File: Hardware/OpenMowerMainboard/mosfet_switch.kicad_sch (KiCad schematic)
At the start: 5 parts, among them Q5 BSS138, Q6 Q_PMOS_GDS

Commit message: wip schematic
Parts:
- renumbered Q5 to Q7, Q6 to Q8, R26 to R29, R27 to R30, R28 to R31
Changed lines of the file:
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@@
   (symbol (lib_id "Device:R") (at 107.95 97.79 0)
     (in_bom yes) (on_board yes) (fields_autoplaced)
-    (property "Reference" "R26" (id 0) (at 110.49 96.5199 0)
+    (property "Reference" "R29" (id 0) (at 110.49 96.5199 0)
       (effects (font (size 1.27 1.27)) (justify left))
     )
@@
   (symbol (lib_id "Device:R") (at 114.3 90.17 90)
     (in_bom yes) (on_board yes) (fields_autoplaced)
-    (property "Reference" "R27" (id 0) (at 114.3 83.82 90))
+    (property "Reference" "R30" (id 0) (at 114.3 83.82 90))
     (property "Value" "R" (id 1) (at 114.3 86.36 90))
     (property "Footprint" "Resistor_SMD:R_0805_2012Metric" (id 2) (at 114.3 91.948 90)
@@
   (symbol (lib_id "Device:Q_PMOS_GDS") (at 135.89 80.01 0)
     (in_bom yes) (on_board yes) (fields_autoplaced)
-    (property "Reference" "Q6" (id 0) (at 142.24 78.7399 0)
+    (property "Reference" "Q8" (id 0) (at 142.24 78.7399 0)
       (effects (font (size 1.27 1.27)) (justify left))
     )
@@
   (symbol (lib_id "Transistor_FET:BSS138") (at 125.73 90.17 0)
     (in_bom yes) (on_board yes) (fields_autoplaced)
-    (property "Reference" "Q5" (id 0) (at 132.08 88.8999 0)
+    (property "Reference" "Q7" (id 0) (at 132.08 88.8999 0)
       (effects (font (size 1.27 1.27)) (justify left))
     )
@@
   (symbol (lib_id "Device:R") (at 128.27 71.12 0)
     (in_bom yes) (on_board yes) (fields_autoplaced)
-    (property "Reference" "R28" (id 0) (at 130.81 69.8499 0)
+    (property "Reference" "R31" (id 0) (at 130.81 69.8499 0)
       (effects (font (size 1.27 1.27)) (justify left))
     )

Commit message: added footprints to schematic
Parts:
- R29, R30, R31: footprint Resistor_SMD:R_0805_2012Metric -> Resistor_SMD:R_0805_2012Metric_Pad1.20x1.40mm_HandSolder
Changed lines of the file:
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@@
       (effects (font (size 1.27 1.27)) (justify left))
     )
-    (property "Footprint" "Resistor_SMD:R_0805_2012Metric" (id 2) (at 106.172 97.79 90)
+    (property "Footprint" "Resistor_SMD:R_0805_2012Metric_Pad1.20x1.40mm_HandSolder" (id 2) (at 106.172 97.79 90)
       (effects (font (size 1.27 1.27)) hide)
     )
@@
     (property "Reference" "R30" (id 0) (at 114.3 83.82 90))
     (property "Value" "R" (id 1) (at 114.3 86.36 90))
-    (property "Footprint" "Resistor_SMD:R_0805_2012Metric" (id 2) (at 114.3 91.948 90)
+    (property "Footprint" "Resistor_SMD:R_0805_2012Metric_Pad1.20x1.40mm_HandSolder" (id 2) (at 114.3 91.948 90)
       (effects (font (size 1.27 1.27)) hide)
     )
@@
       (effects (font (size 1.27 1.27)) (justify left))
     )
-    (property "Footprint" "Resistor_SMD:R_0805_2012Metric" (id 2) (at 126.492 71.12 90)
+    (property "Footprint" "Resistor_SMD:R_0805_2012Metric_Pad1.20x1.40mm_HandSolder" (id 2) (at 126.492 71.12 90)
       (effects (font (size 1.27 1.27)) hide)
     )

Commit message: wip
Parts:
- renumbered Q7 to Q5, Q8 to Q6, R29 to R26, R30 to R27, R31 to R28
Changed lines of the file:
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@@
   (symbol (lib_id "Device:R") (at 107.95 97.79 0)
     (in_bom yes) (on_board yes) (fields_autoplaced)
-    (property "Reference" "R29" (id 0) (at 110.49 96.5199 0)
+    (property "Reference" "R26" (id 0) (at 110.49 96.5199 0)
       (effects (font (size 1.27 1.27)) (justify left))
     )
@@
   (symbol (lib_id "Device:R") (at 114.3 90.17 90)
     (in_bom yes) (on_board yes) (fields_autoplaced)
-    (property "Reference" "R30" (id 0) (at 114.3 83.82 90))
+    (property "Reference" "R27" (id 0) (at 114.3 83.82 90))
     (property "Value" "R" (id 1) (at 114.3 86.36 90))
     (property "Footprint" "Resistor_SMD:R_0805_2012Metric_Pad1.20x1.40mm_HandSolder" (id 2) (at 114.3 91.948 90)
@@
   (symbol (lib_id "Device:Q_PMOS_GDS") (at 135.89 80.01 0)
     (in_bom yes) (on_board yes) (fields_autoplaced)
-    (property "Reference" "Q8" (id 0) (at 142.24 78.7399 0)
+    (property "Reference" "Q6" (id 0) (at 142.24 78.7399 0)
       (effects (font (size 1.27 1.27)) (justify left))
     )
@@
   (symbol (lib_id "Transistor_FET:BSS138") (at 125.73 90.17 0)
     (in_bom yes) (on_board yes) (fields_autoplaced)
-    (property "Reference" "Q7" (id 0) (at 132.08 88.8999 0)
+    (property "Reference" "Q5" (id 0) (at 132.08 88.8999 0)
       (effects (font (size 1.27 1.27)) (justify left))
     )
@@
   (symbol (lib_id "Device:R") (at 128.27 71.12 0)
     (in_bom yes) (on_board yes) (fields_autoplaced)
-    (property "Reference" "R31" (id 0) (at 130.81 69.8499 0)
+    (property "Reference" "R28" (id 0) (at 130.81 69.8499 0)
       (effects (font (size 1.27 1.27)) (justify left))
     )

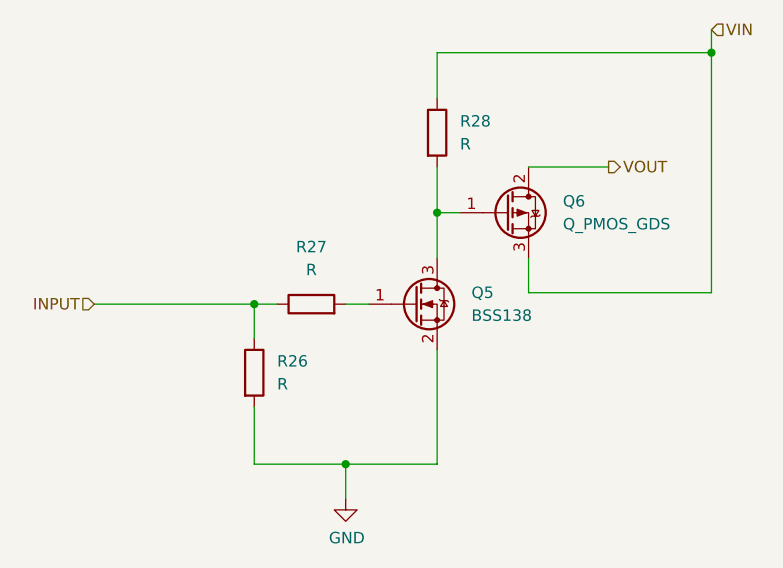
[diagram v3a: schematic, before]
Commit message: update Resistance Values
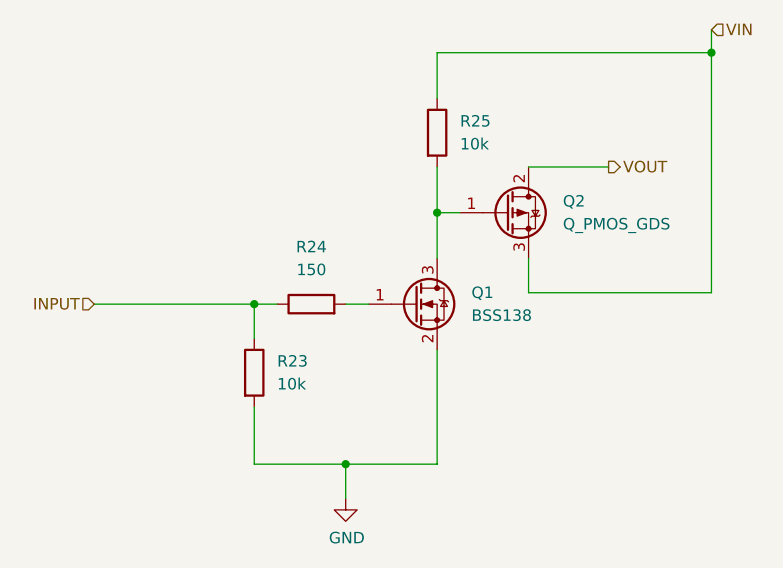
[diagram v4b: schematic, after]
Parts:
- R23: renamed from R26; value R -> 10k
- R24: renamed from R27; value R -> 150
- R25: renamed from R28; value R -> 10k
- renumbered Q5 to Q1, Q6 to Q2
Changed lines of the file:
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@@
   (symbol (lib_id "Device:R") (at 107.95 97.79 0)
     (in_bom yes) (on_board yes) (fields_autoplaced)
-    (property "Reference" "R26" (id 0) (at 110.49 96.5199 0)
+    (property "Reference" "R23" (id 0) (at 110.49 96.5199 0)
       (effects (font (size 1.27 1.27)) (justify left))
     )
-    (property "Value" "R" (id 1) (at 110.49 99.0599 0)
+    (property "Value" "10k" (id 1) (at 110.49 99.0599 0)
       (effects (font (size 1.27 1.27)) (justify left))
     )
@@
   (symbol (lib_id "Device:R") (at 114.3 90.17 90)
     (in_bom yes) (on_board yes) (fields_autoplaced)
-    (property "Reference" "R27" (id 0) (at 114.3 83.82 90))
-    (property "Value" "R" (id 1) (at 114.3 86.36 90))
+    (property "Reference" "R24" (id 0) (at 114.3 83.82 90))
+    (property "Value" "150" (id 1) (at 114.3 86.36 90))
     (property "Footprint" "Resistor_SMD:R_0805_2012Metric_Pad1.20x1.40mm_HandSolder" (id 2) (at 114.3 91.948 90)
       (effects (font (size 1.27 1.27)) hide)
@@
   (symbol (lib_id "Device:Q_PMOS_GDS") (at 135.89 80.01 0)
     (in_bom yes) (on_board yes) (fields_autoplaced)
-    (property "Reference" "Q6" (id 0) (at 142.24 78.7399 0)
+    (property "Reference" "Q2" (id 0) (at 142.24 78.7399 0)
       (effects (font (size 1.27 1.27)) (justify left))
     )
@@
   (symbol (lib_id "Transistor_FET:BSS138") (at 125.73 90.17 0)
     (in_bom yes) (on_board yes) (fields_autoplaced)
-    (property "Reference" "Q5" (id 0) (at 132.08 88.8999 0)
+    (property "Reference" "Q1" (id 0) (at 132.08 88.8999 0)
       (effects (font (size 1.27 1.27)) (justify left))
     )
@@
   (symbol (lib_id "Device:R") (at 128.27 71.12 0)
     (in_bom yes) (on_board yes) (fields_autoplaced)
-    (property "Reference" "R28" (id 0) (at 130.81 69.8499 0)
+    (property "Reference" "R25" (id 0) (at 130.81 69.8499 0)
       (effects (font (size 1.27 1.27)) (justify left))
     )
-    (property "Value" "R" (id 1) (at 130.81 72.3899 0)
+    (property "Value" "10k" (id 1) (at 130.81 72.3899 0)
       (effects (font (size 1.27 1.27)) (justify left))
     )

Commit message: added todos, added image of current mainboard
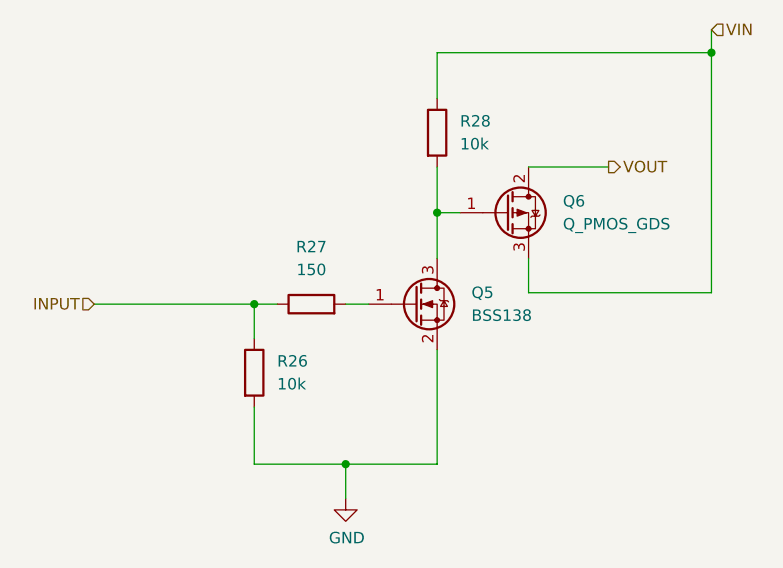
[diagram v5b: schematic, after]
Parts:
- renumbered Q1 to Q5, Q2 to Q6, R23 to R26, R24 to R27, R25 to R28
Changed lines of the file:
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@@
   (symbol (lib_id "Device:R") (at 107.95 97.79 0)
     (in_bom yes) (on_board yes) (fields_autoplaced)
-    (property "Reference" "R23" (id 0) (at 110.49 96.5199 0)
+    (property "Reference" "R26" (id 0) (at 110.49 96.5199 0)
       (effects (font (size 1.27 1.27)) (justify left))
     )
@@
   (symbol (lib_id "Device:R") (at 114.3 90.17 90)
     (in_bom yes) (on_board yes) (fields_autoplaced)
-    (property "Reference" "R24" (id 0) (at 114.3 83.82 90))
+    (property "Reference" "R27" (id 0) (at 114.3 83.82 90))
     (property "Value" "150" (id 1) (at 114.3 86.36 90))
     (property "Footprint" "Resistor_SMD:R_0805_2012Metric_Pad1.20x1.40mm_HandSolder" (id 2) (at 114.3 91.948 90)
@@
   (symbol (lib_id "power:GND") (at 118.11 111.76 0)
     (in_bom yes) (on_board yes)
-    (property "Reference" "#PWR0126" (id 0) (at 118.11 118.11 0)
+    (property "Reference" "#PWR0125" (id 0) (at 118.11 118.11 0)
       (effects (font (size 1.27 1.27)) hide)
     )
@@
   (symbol (lib_id "Device:Q_PMOS_GDS") (at 135.89 80.01 0)
     (in_bom yes) (on_board yes) (fields_autoplaced)
-    (property "Reference" "Q2" (id 0) (at 142.24 78.7399 0)
+    (property "Reference" "Q6" (id 0) (at 142.24 78.7399 0)
       (effects (font (size 1.27 1.27)) (justify left))
     )
@@
   (symbol (lib_id "Transistor_FET:BSS138") (at 125.73 90.17 0)
     (in_bom yes) (on_board yes) (fields_autoplaced)
-    (property "Reference" "Q1" (id 0) (at 132.08 88.8999 0)
+    (property "Reference" "Q5" (id 0) (at 132.08 88.8999 0)
       (effects (font (size 1.27 1.27)) (justify left))
     )
@@
   (symbol (lib_id "Device:R") (at 128.27 71.12 0)
     (in_bom yes) (on_board yes) (fields_autoplaced)
-    (property "Reference" "R25" (id 0) (at 130.81 69.8499 0)
+    (property "Reference" "R28" (id 0) (at 130.81 69.8499 0)
       (effects (font (size 1.27 1.27)) (justify left))
     )

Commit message: BoM data added to kicad - results exported to .xlsx file
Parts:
- Q5: LCSC (none) -> C360338; Part Number (none) -> AP2300; Stock_PN (none) -> Q-AP2300
- Q6: Digikey (none) -> IRFR5505PBFCT-ND; Part Number (none) -> IRFR5505TRPBF; Stock_PN (none) -> Q-IRFR5505TRPBF
- R26, R28: Digikey (none) -> 738-RMCF0805FG10K0CT-ND; Part Number (none) -> RMCF0805FG10K0; Stock_PN (none) -> R-805-10K-.125W-1%
- R27: Digikey (none) -> 311-150CRCT-ND; Part Number (none) -> RC0805FR-07150RL; Stock_PN (none) -> R-805-150-.125W-1%
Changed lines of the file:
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@@
+      (effects (font (size 1.27 1.27)) hide)
+    )
+    (property "Digikey" "738-RMCF0805FG10K0CT-ND" (id 4) (at 107.95 97.79 0)
+      (effects (font (size 1.27 1.27)) hide)
+    )
+    (property "Part Number" "RMCF0805FG10K0" (id 5) (at 107.95 97.79 0)
+      (effects (font (size 1.27 1.27)) hide)
+    )
+    (property "Stock_PN" "R-805-10K-.125W-1%" (id 6) (at 107.95 97.79 0)
       (effects (font (size 1.27 1.27)) hide)
     )
@@
     )
     (property "Datasheet" "~" (id 3) (at 114.3 90.17 0)
+      (effects (font (size 1.27 1.27)) hide)
+    )
+    (property "Stock_PN" "R-805-150-.125W-1%" (id 4) (at 114.3 90.17 0)
+      (effects (font (size 1.27 1.27)) hide)
+    )
+    (property "Digikey" "311-150CRCT-ND" (id 5) (at 114.3 90.17 0)
+      (effects (font (size 1.27 1.27)) hide)
+    )
+    (property "Part Number" "RC0805FR-07150RL" (id 6) (at 114.3 90.17 0)
       (effects (font (size 1.27 1.27)) hide)
     )
@@
       (effects (font (size 1.27 1.27)) hide)
     )
+    (property "Digikey" "IRFR5505PBFCT-ND" (id 4) (at 135.89 80.01 0)
+      (effects (font (size 1.27 1.27)) hide)
+    )
+    (property "Part Number" "IRFR5505TRPBF" (id 5) (at 135.89 80.01 0)
+      (effects (font (size 1.27 1.27)) hide)
+    )
+    (property "Stock_PN" "Q-IRFR5505TRPBF" (id 6) (at 135.89 80.01 0)
+      (effects (font (size 1.27 1.27)) hide)
+    )
     (pin "1")
     (pin "2")
@@
     (property "Datasheet" "https://www.onsemi.com/pub/Collateral/BSS138-D.PDF" (id 3) (at 125.73 90.17 0)
       (effects (font (size 1.27 1.27)) (justify left) hide)
+    )
+    (property "LCSC" "C360338" (id 4) (at 125.73 90.17 0)
+      (effects (font (size 1.27 1.27)) hide)
+    )
+    (property "Part Number" "AP2300" (id 5) (at 125.73 90.17 0)
+      (effects (font (size 1.27 1.27)) hide)
+    )
+    (property "Stock_PN" "Q-AP2300" (id 6) (at 125.73 90.17 0)
+      (effects (font (size 1.27 1.27)) hide)
     )
     (pin "1")
@@
       (effects (font (size 1.27 1.27)) hide)
     )
+    (property "Digikey" "738-RMCF0805FG10K0CT-ND" (id 4) (at 128.27 71.12 0)
+      (effects (font (size 1.27 1.27)) hide)
+    )
+    (property "Part Number" "RMCF0805FG10K0" (id 5) (at 128.27 71.12 0)
+      (effects (font (size 1.27 1.27)) hide)
+    )
+    (property "Stock_PN" "R-805-10K-.125W-1%" (id 6) (at 128.27 71.12 0)
+      (effects (font (size 1.27 1.27)) hide)
+    )

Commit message: BOM changes
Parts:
- Q5: Digikey (none) -> BSS138K-13DICT-ND
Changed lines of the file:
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@@
+      (effects (font (size 1.27 1.27)) hide)
+    )
+    (property "Digikey" "BSS138K-13DICT-ND" (id 7) (at 125.73 90.17 0)
       (effects (font (size 1.27 1.27)) hide)
     )
